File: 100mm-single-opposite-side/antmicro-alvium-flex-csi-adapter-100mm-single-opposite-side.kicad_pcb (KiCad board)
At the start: 2 copper layers, 25.5 x 100.1 mm, 2 parts, among them J1 WE_687622100002_FLEX, J2 WE_687650100002_FLEX

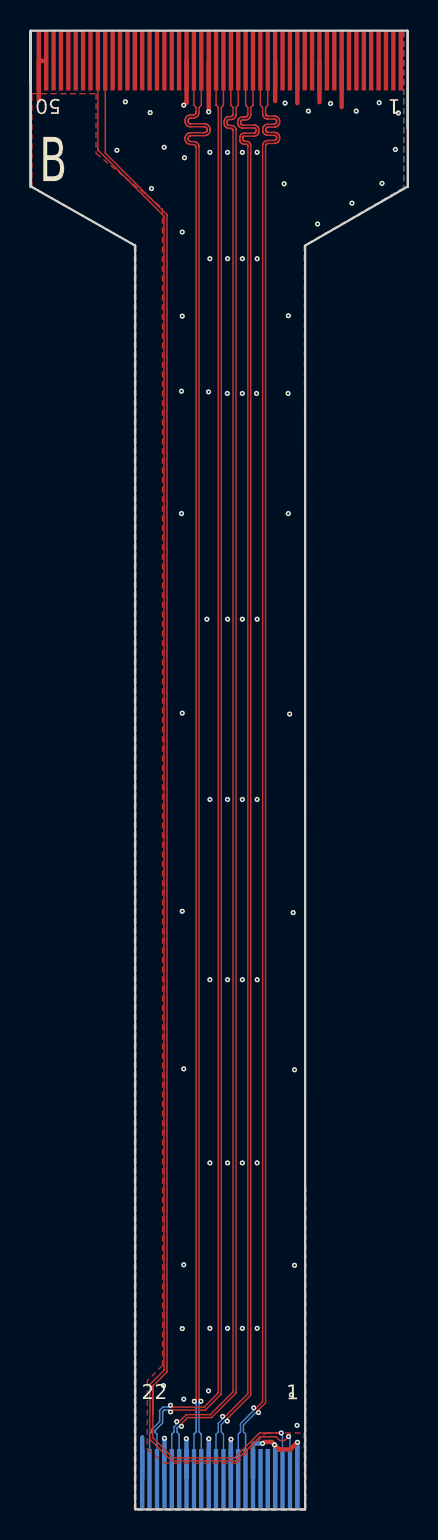
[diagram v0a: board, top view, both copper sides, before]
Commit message: 100mm-single-opposite: update signage
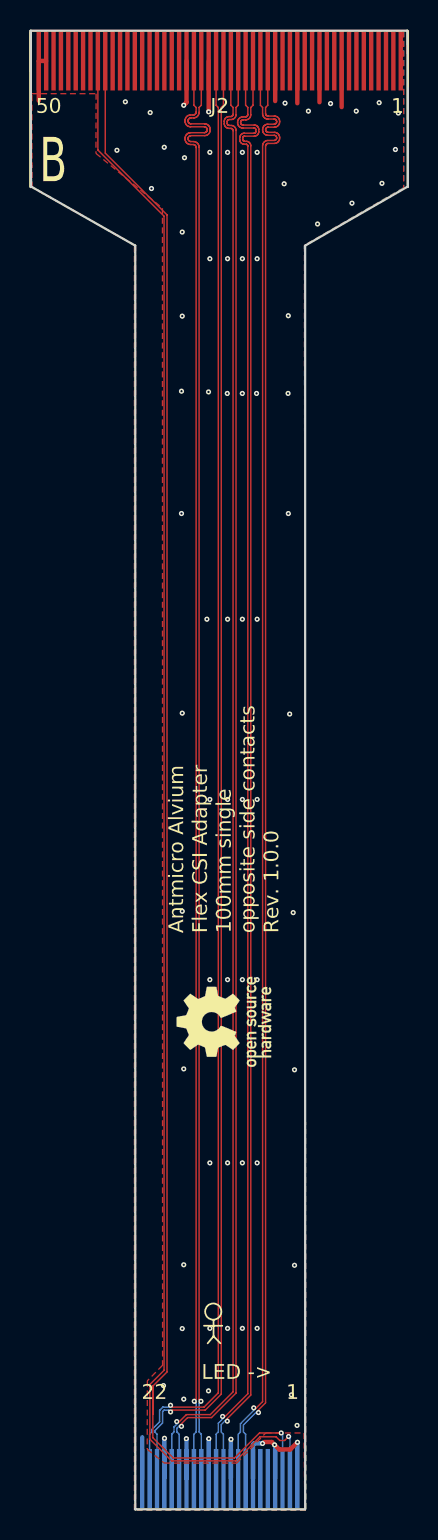
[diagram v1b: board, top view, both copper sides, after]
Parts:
- added N1: oshw_logo, antmicro-alvium-flex-csi-adapter-footprints:oshw-logo, F.Cu at (189.0, 131.8)
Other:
- board text added: "Antmicro Alvium Flex CSI Adapter 100mm single opposite side contacts Rev. 1.0.0"
- board text added: "LED ->"

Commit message: Remove obsolete markings
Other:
- board text added: "Antmicro Alvium Flex CSI Adapter 100mm single opposite side contacts Rev. 1.0.1"
- board text removed: "Antmicro Alvium Flex CSI Adapter 100mm single opposite side contacts Rev. 1.0.0"
- board text removed: "B"
